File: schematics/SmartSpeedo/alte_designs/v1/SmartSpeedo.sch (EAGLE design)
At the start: 145 parts, among them IC1 4093D, IC2 L9637D, IC4 ATMEGA2560-16AU, T1 BC847, T13 Mouser: 771-2N7002BK215 , N-C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, T2 BC847, U4 MCP2515, U5 MCP2551

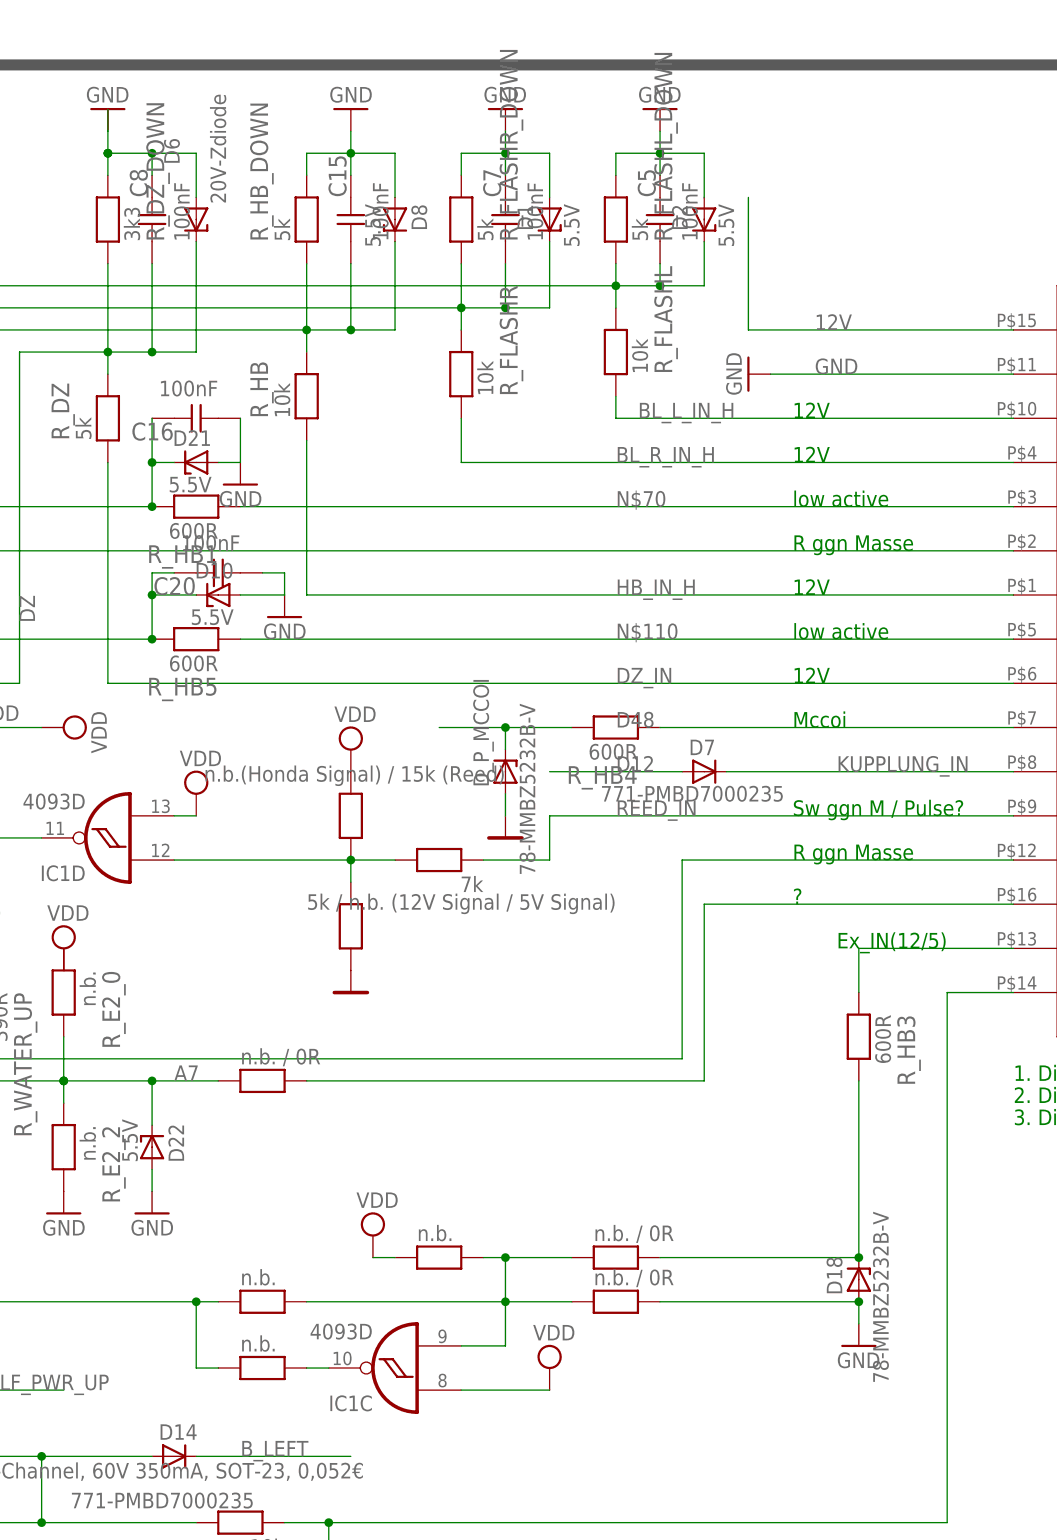
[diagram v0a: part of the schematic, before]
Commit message: Repaired Design (5V Diode)
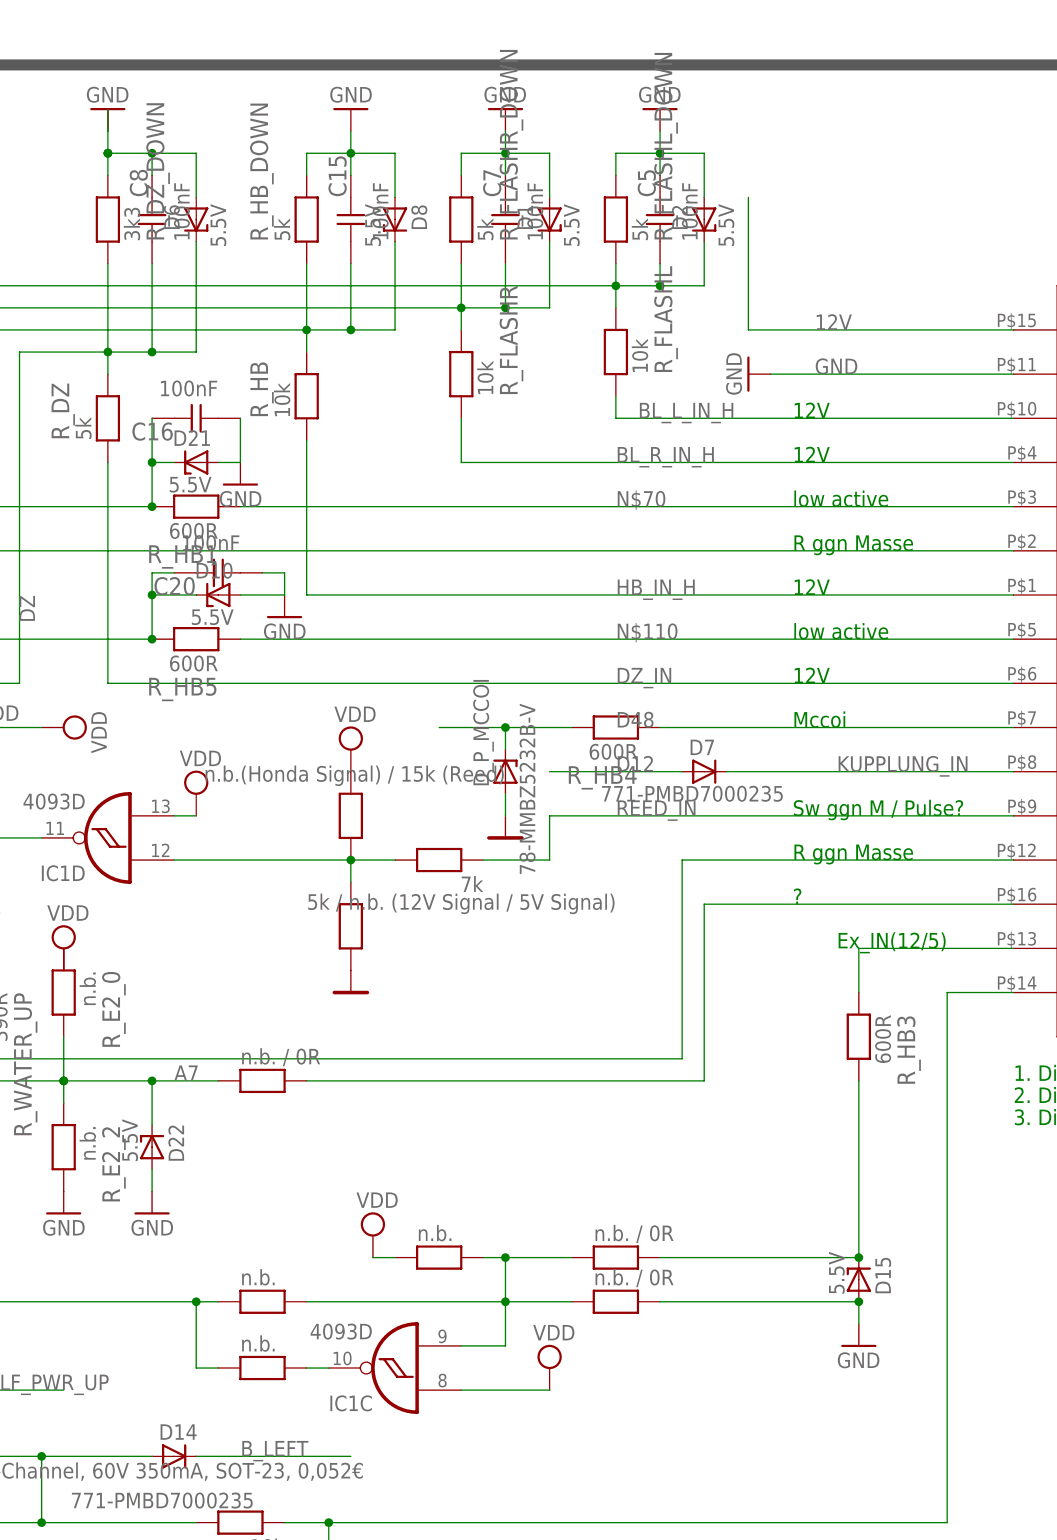
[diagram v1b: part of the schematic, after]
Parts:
- D15: value 78-MMBZ5232B-V -> 5.5V
- D6: value 20V-Zdiode -> 5.5V
- renumbered D18 to D15
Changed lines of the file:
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@@
 <?xml version="1.0" encoding="utf-8"?>
 <!DOCTYPE eagle SYSTEM "eagle.dtd">
-<eagle version="6.5.0">
+<eagle version="6.4">
 <drawing>
 <settings>
@@
 <part name="RX_H" library="resistor" deviceset="R-EU_" device="M0805" value="1k2"/>
 <part name="GND9" library="SparkFun" deviceset="GND" device=""/>
-<part name="D6" library="diode" deviceset="ZENER-DIODE" device="SOT23" value="20V-Zdiode"/>
 <part name="GND12" library="SparkFun" deviceset="GND" device=""/>
 <part name="GND14" library="SparkFun" deviceset="GND" device=""/>
@@
 <part name="R_REED" library="RCLDT" deviceset="R" device="0805" value="7k "/>
 <part name="D_VERPOL" library="RCLDT" deviceset="D-S" device="SMB-A+K" value="SS24T3G"/>
-<part name="D18" library="diode" deviceset="ZENER-DIODE" device="SOT23" value="78-MMBZ5232B-V"/>
 <part name="GND6" library="supply1" deviceset="GND" device=""/>
 <part name="R_V_LOW" library="RCLDT" deviceset="R" device="0805" value="1k"/>
@@
 <part name="500MA_LITTLEFUSE" library="resistor" deviceset="R-EU_" device="R1210" value="1210L050YR"/>
 <part name="700MA_LITTLEFUSE" library="resistor" deviceset="R-EU_" device="R1210" value="1210L075YR"/>
+<part name="D6" library="diode" deviceset="ZENER-DIODE" device="SOT23" value="5.5V"/>
+<part name="D15" library="diode" deviceset="ZENER-DIODE" device="SOT23" value="5.5V"/>
 </parts>
 <sheets>
@@
 <instance part="RX_H" gate="G$1" x="-33.02" y="160.02" rot="R270"/>
 <instance part="GND9" gate="1" x="-33.02" y="137.16"/>
-<instance part="D6" gate="G$1" x="91.44" y="236.22" smashed="yes" rot="MR270">
-<attribute name="NAME" x="89.535" y="245.618" size="1.778" layer="95" rot="MR270"/>
-<attribute name="VALUE" x="94.869" y="250.698" size="1.778" layer="96" rot="MR270"/>
-</instance>
 <instance part="GND12" gate="1" x="-307.34" y="215.9"/>
 <instance part="GND14" gate="1" x="-279.4" y="200.66" rot="R270"/>
@@
 <attribute name="NAME" x="-29.845" y="20.32" size="2.032" layer="95"/>
 <attribute name="VALUE" x="-29.845" y="17.78" size="1.778" layer="96"/>
-</instance>
-<instance part="D18" gate="G$1" x="167.64" y="114.3" smashed="yes" rot="R90">
-<attribute name="NAME" x="165.735" y="112.522" size="1.778" layer="95" rot="R90"/>
-<attribute name="VALUE" x="171.069" y="102.362" size="1.778" layer="96" rot="R90"/>
 </instance>
 <instance part="GND6" gate="1" x="167.64" y="106.68"/>
@@
 <instance part="500MA_LITTLEFUSE" gate="G$1" x="139.7" y="33.02"/>
 <instance part="700MA_LITTLEFUSE" gate="G$1" x="-12.7" y="15.24"/>
+<instance part="D6" gate="G$1" x="91.44" y="236.22" rot="MR270"/>
+<instance part="D15" gate="G$1" x="167.64" y="114.3" rot="MR90"/>
 </instances>
 <busses>
@@
 <segment>
 <pinref part="GND1" gate="1" pin="GND"/>
-<pinref part="D6" gate="G$1" pin="A"/>
 <wire x1="91.44" y1="238.76" x2="91.44" y2="243.84" width="0.1524" layer="91"/>
 <wire x1="91.44" y1="243.84" x2="86.36" y2="243.84" width="0.1524" layer="91"/>
@@
 <wire x1="81.28" y1="246.38" x2="81.28" y2="248.92" width="0.1524" layer="91"/>
 <junction x="86.36" y="243.84"/>
+<pinref part="D6" gate="G$1" pin="A"/>
 </segment>
 <segment>
@@
 <wire x1="167.64" y1="109.22" x2="167.64" y2="111.76" width="0.1524" layer="91"/>
 <pinref part="GND6" gate="1" pin="GND"/>
-<pinref part="D18" gate="G$1" pin="A"/>
 <wire x1="144.78" y1="111.76" x2="167.64" y2="111.76" width="0.1524" layer="91"/>
+<pinref part="R_E1_3" gate="G$1" pin="1"/>
+<pinref part="D15" gate="G$1" pin="A"/>
 <junction x="167.64" y="111.76"/>
-<pinref part="R_E1_3" gate="G$1" pin="1"/>
 </segment>
 <segment>
@@
 <label x="71.12" y="193.04" size="1.778" layer="95" rot="R270"/>
 <pinref part="R_DZ" gate="G$1" pin="2"/>
-<pinref part="D6" gate="G$1" pin="C"/>
 <pinref part="IC1" gate="A" pin="I1"/>
 <pinref part="R_DZ_DOWN" gate="G$1" pin="1"/>
@@
 <junction x="81.28" y="220.98"/>
 <junction x="86.36" y="220.98"/>
+<pinref part="D6" gate="G$1" pin="C"/>
 </segment>
 </net>
@@
 <segment>
 <pinref part="R_HB3" gate="G$1" pin="2"/>
-<pinref part="D18" gate="G$1" pin="C"/>
 <pinref part="R_E1_1" gate="G$1" pin="1"/>
 <wire x1="167.64" y1="116.84" x2="167.64" y2="137.16" width="0.1524" layer="91"/>
 <wire x1="167.64" y1="116.84" x2="144.78" y2="116.84" width="0.1524" layer="91"/>
+<pinref part="D15" gate="G$1" pin="C"/>
 <junction x="167.64" y="116.84"/>
 </segment>
